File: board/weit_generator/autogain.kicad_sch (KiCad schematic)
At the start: 11 parts, among them U3 TL431DBZ

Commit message: .
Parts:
- removed U3: TL431DBZ, Package_TO_SOT_SMD:SOT-23, symbol Reference_Voltage:TL431DBZ
- removed U? (x2): MCP6004, Package_SO:SOIC-14_3.9x8.7mm_P1.27mm, symbol Amplifier_Operational:MCP6004
- added U1: MCP6004, Package_DIP:DIP-14_W7.62mm_Socket_LongPads, symbol Amplifier_Operational:MCP6004
- added U3: LM4041LP-ADJ, Package_TO_SOT_THT:TO-92_Inline, symbol Reference_Voltage:LM4041LP-ADJ
- C12: footprint (none) -> Capacitor_SMD:C_0805_2012Metric_Pad1.18x1.45mm_HandSolder
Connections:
- net GND: now also U3.3 (A)
- net IN: now also U1.12 (+)
- net at C?.2, D2.1 (K), R?.2: now also U1.13 (-), U1.3 (+)
- net at D2.2 (A): now also U1.14
- net at C12.1, R25.1: now also U1.1
- net at C12.2, C?.1, RV?.2: now also U1.2 (-)
- net at R?.2, RV?.3: now also U3.2 (K)
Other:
- note added: "Low leakage PP capacitor + 1M resistor for stable decay time"
- note removed: "Low leakage PP capacitor + 1M resistor create predictable decay time"

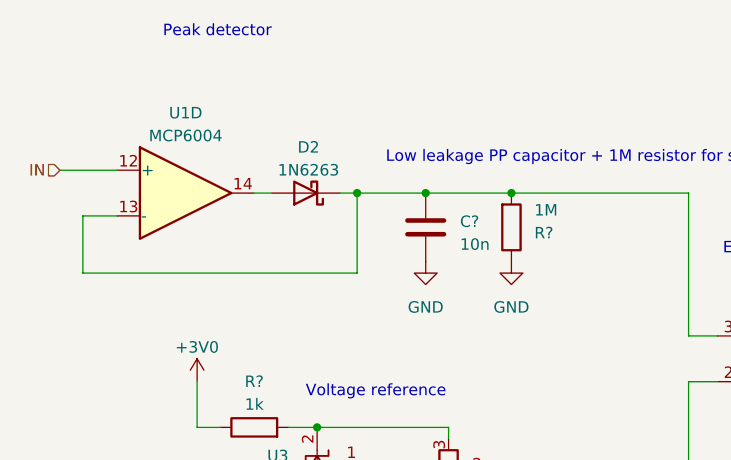
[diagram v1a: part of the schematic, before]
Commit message: added filtering
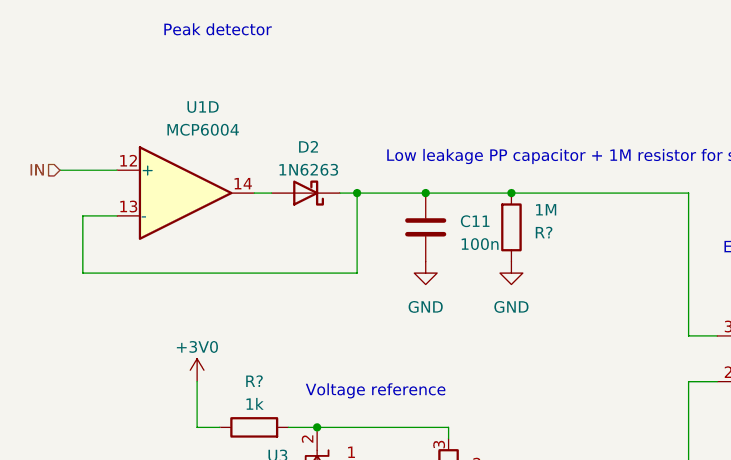
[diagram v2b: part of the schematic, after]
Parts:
- removed C?: 10n, Capacitor_THT:C_Rect_L9.0mm_W4.0mm_P7.50mm_MKT, symbol Device:C
- added C11: 100n, Capacitor_THT:C_Rect_L13.0mm_W6.0mm_P10.00mm_FKS3_FKP3_MKS4, symbol Device:C
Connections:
- net GND: now also C11.1
- net at D2.1 (K), R?.2, U1.13 (-)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: now also C11.2
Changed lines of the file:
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@@
   (junction (at 118.11 77.47) (diameter 0) (color 0 0 0 0)
   )
+  (junction (at 125.73 77.47) (diameter 0) (color 0 0 0 0)
+  )
   (junction (at 154.94 108.585) (diameter 0) (color 0 0 0 0)
   )
-  (junction (at 125.73 77.47) (diameter 0) (color 0 0 0 0)
-  )
   (junction (at 134.62 108.585) (diameter 0) (color 0 0 0 0)
   )
@@
     (stroke (width 0) (type default))
   )
+  (wire (pts (xy 118.11 77.47) (xy 125.73 77.47))
+    (stroke (width 0) (type default))
+  )
+  (wire (pts (xy 134.62 108.585) (xy 154.94 108.585))
+    (stroke (width 0) (type default))
+  )
+  (wire (pts (xy 87.63 86.36) (xy 87.63 80.01))
+    (stroke (width 0) (type default))
+  )
+  (wire (pts (xy 154.94 98.425) (xy 158.115 98.425))
+    (stroke (width 0) (type default))
+  )
+  (wire (pts (xy 169.545 108.585) (xy 175.26 108.585))
+    (stroke (width 0) (type default))
+  )
+  (wire (pts (xy 100.33 103.505) (xy 102.87 103.505))
+    (stroke (width 0) (type default))
+  )
+  (wire (pts (xy 118.11 86.36) (xy 87.63 86.36))
+    (stroke (width 0) (type default))
+  )
+  (wire (pts (xy 87.63 80.01) (xy 91.44 80.01))
+    (stroke (width 0) (type default))
+  )
   (wire (pts (xy 125.73 77.47) (xy 135.255 77.47))
     (stroke (width 0) (type default))
   )
-  (wire (pts (xy 134.62 108.585) (xy 154.94 108.585))
-    (stroke (width 0) (type default))
-  )
-  (wire (pts (xy 87.63 86.36) (xy 87.63 80.01))
-    (stroke (width 0) (type default))
-  )
-  (wire (pts (xy 154.94 98.425) (xy 158.115 98.425))
-    (stroke (width 0) (type default))
-  )
-  (wire (pts (xy 169.545 108.585) (xy 175.26 108.585))
-    (stroke (width 0) (type default))
-  )
-  (wire (pts (xy 100.33 103.505) (xy 102.87 103.505))
-    (stroke (width 0) (type default))
-  )
-  (wire (pts (xy 118.11 86.36) (xy 87.63 86.36))
-    (stroke (width 0) (type default))
-  )
-  (wire (pts (xy 87.63 80.01) (xy 91.44 80.01))
-    (stroke (width 0) (type default))
-  )
   (wire (pts (xy 173.355 95.885) (xy 175.26 95.885))
     (stroke (width 0) (type default))
@@
   )
   (wire (pts (xy 110.49 103.505) (xy 113.665 103.505))
-    (stroke (width 0) (type default))
-  )
-  (wire (pts (xy 118.11 77.47) (xy 125.73 77.47))
     (stroke (width 0) (type default))
   )
@@
   (hierarchical_label "IN" (shape input) (at 85.09 74.93 180) (fields_autoplaced)
     (effects (font (size 1.27 1.27)) (justify right))
+  )
+  (symbol (lib_id "Device:C") (at 125.73 81.28 180) (unit 1)
+    (in_bom yes) (on_board yes) (dnp no) (fields_autoplaced)
+    (property "Reference" "C11" (at 129.54 80.645 0)
+      (effects (font (size 1.27 1.27)) (justify right))
+    )
+    (property "Value" "100n" (at 129.54 83.185 0)
+      (effects (font (size 1.27 1.27)) (justify right))
+    )
+    (property "Footprint" "Capacitor_THT:C_Rect_L13.0mm_W6.0mm_P10.00mm_FKS3_FKP3_MKS4" (at 124.7648 77.47 0)
+      (effects (font (size 1.27 1.27)) hide)
+    )
+    (property "Datasheet" "~" (at 125.73 81.28 0)
+      (effects (font (size 1.27 1.27)) hide)
+    )
+    (pin "1")
+    (pin "2")
+    (instances
+      (project "weit_generator"
+        (path "/b85c55a9-e1f6-4dbf-a795-73634abf8d52"
+          (reference "C11") (unit 1)
+        )
+        (path "/b85c55a9-e1f6-4dbf-a795-73634abf8d52/97b440c2-49e0-43c1-8dbd-070a3fa32fe0"
+          (reference "C6") (unit 1)
+        )
+      )
+    )
   )
   (symbol (lib_id "Diode:1N6263") (at 112.395 77.47 180) (unit 1)
@@
   )
   (symbol (lib_id "Amplifier_Operational:MCP6004") (at 99.06 77.47 0) (unit 4)
-    (in_bom yes) (on_board yes) (dnp no) (fields_autoplaced)
-    (property "Reference" "U1" (at 99.06 68.58 0)
-      (effects (font (size 1.27 1.27)))
-    )
-    (property "Value" "MCP6004" (at 99.06 71.12 0)
+    (in_bom yes) (on_board yes) (dnp no)
+    (property "Reference" "U1" (at 100.965 67.945 0)
+      (effects (font (size 1.27 1.27)))
+    )
+    (property "Value" "MCP6004" (at 100.965 70.485 0)
       (effects (font (size 1.27 1.27)))
     )
@@
         )
       )
-    )
-  )
-  (symbol (lib_id "Device:C") (at 125.73 81.28 180) (unit 1)
-    (in_bom yes) (on_board yes) (dnp no)
-    (property "Reference" "C?" (at 129.54 80.645 0)
-      (effects (font (size 1.27 1.27)) (justify right))
-    )
-    (property "Value" "10n" (at 129.54 83.185 0)
-      (effects (font (size 1.27 1.27)) (justify right))
-    )
-    (property "Footprint" "Capacitor_THT:C_Rect_L9.0mm_W4.0mm_P7.50mm_MKT" (at 124.7648 77.47 0)
-      (effects (font (size 1.27 1.27)) hide)
-    )
-    (property "Datasheet" "~" (at 125.73 81.28 0)
-      (effects (font (size 1.27 1.27)) hide)
-    )
-    (pin "1")
-    (pin "2")
-    (instances
-      (project "weit_generator"
-        (path "/b85c55a9-e1f6-4dbf-a795-73634abf8d52"
-          (reference "C?") (unit 1)
-        )
-        (path "/b85c55a9-e1f6-4dbf-a795-73634abf8d52/97b440c2-49e0-43c1-8dbd-070a3fa32fe0"
-          (reference "C9") (unit 1)
-        )
-      )

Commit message: hopefully repaired instability
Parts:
- removed C12: 1n, Capacitor_SMD:C_0805_2012Metric_Pad1.18x1.45mm_HandSolder, symbol Device:C
- removed C?: 100n, Capacitor_SMD:C_0805_2012Metric_Pad1.18x1.45mm_HandSolder, symbol Device:C
- removed R?: 1k, Resistor_SMD:R_0805_2012Metric_Pad1.20x1.40mm_HandSolder, symbol Device:R
- removed RV?: 10k, Potentiometer_THT:Potentiometer_Bourns_3266Y_Vertical, symbol Device:R_Potentiometer
- removed U3: LM4041LP-ADJ, Package_TO_SOT_THT:TO-92_Inline, symbol Reference_Voltage:LM4041LP-ADJ
- added C7: 100u, symbol Device:C_Polarized
- added C?: 10n, Capacitor_THT:C_Rect_L9.0mm_W4.0mm_P7.50mm_MKT, symbol Device:C
- added Q1: BC547, Package_TO_SOT_THT:TO-92_Inline, symbol Transistor_BJT:BC547
- added R21: 100k, Resistor_THT:R_Axial_DIN0207_L6.3mm_D2.5mm_P2.54mm_Vertical, symbol Device:R
- added R?: 1M, Resistor_THT:R_Axial_DIN0207_L6.3mm_D2.5mm_P2.54mm_Vertical, symbol Device:R
- added R? (x2): 100k, Resistor_SMD:R_0805_2012Metric_Pad1.20x1.40mm_HandSolder, symbol Device:R
- added RV?: 10k, Potentiometer_THT:Potentiometer_Bourns_3266Y_Vertical, symbol Device:R_Potentiometer
- C11: value 100n -> 10n
- R25: value 1k -> 100
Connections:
- net GND: now also C7.2, Q1.3 (E), R?.1, R?.1
- net IN: now also C?.2; no longer U1.12 (+)
- net OUT: now also R25.1; no longer R25.2
- net at U1.1: now also RV?.2; no longer R25.1
- net Vref: now reaches U1.2 (-)
- new net: C7.1, R21.1, R?.2, RV?.3
- new net: C?.1, R?.2, R?.2, U1.12 (+)
- new net: Q1.1 (C), R25.2
- new net: Q1.2 (B), R21.2
- new net +1V2: R?.1
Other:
- note removed: "Voltage reference"
- moved on the sheet: R25, R?

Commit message: New layout
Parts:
- removed C?: 10n, Capacitor_THT:C_Rect_L9.0mm_W4.0mm_P7.50mm_MKT, symbol Device:C
- removed R? (x2): 100k, Resistor_SMD:R_0805_2012Metric_Pad1.20x1.40mm_HandSolder, symbol Device:R
- removed U1: MCP6004, Package_DIP:DIP-14_W7.62mm_Socket_LongPads, symbol Amplifier_Operational:MCP6004
- added C11: 1u, Capacitor_THT:C_Rect_L7.2mm_W4.5mm_P5.00mm_FKS2_FKP2_MKS2_MKP2, symbol Device:C
- added C12: 22u, Capacitor_THT:CP_Radial_D6.3mm_P2.50mm, symbol Device:C_Polarized
- added R24: 100, Resistor_THT:R_Axial_DIN0207_L6.3mm_D2.5mm_P2.54mm_Vertical, symbol Device:R
- added R26: 10k, Resistor_THT:R_Axial_DIN0207_L6.3mm_D2.5mm_P2.54mm_Vertical, symbol Device:R
- added R?: 1M, Resistor_THT:R_Axial_DIN0207_L6.3mm_D2.5mm_P2.54mm_Vertical, symbol Device:R
- added RV1: 10k, Potentiometer_THT:Potentiometer_Bourns_3266Y_Vertical, symbol Device:R_Potentiometer
- added TP1 (x2): TestPoint, TestPoint:TestPoint_Pad_D3.0mm, symbol Connector:TestPoint
- added U? (x2): MCP6004, Package_DIP:DIP-14_W7.62mm_Socket, symbol Amplifier_Operational:MCP6004
- C13: renamed from C7; footprint (none) -> Capacitor_THT:CP_Radial_D6.3mm_P2.50mm
- C?: renamed from C11; footprint Capacitor_THT:C_Rect_L13.0mm_W6.0mm_P10.00mm_FKS3_FKP3_MKS4 -> Capacitor_THT:C_Rect_L13.0mm_W4.0mm_P10.00mm_FKS3_FKP3_MKS4; Dielectric (none) -> Polistyrene
- R28: renamed from R21; value 100k -> 100
- renumbered R25 to R29
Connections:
- net +1V2: now also RV1.3
- net GND: now also RV1.1
- net IN: now also R?.2
- net at C?.2, R?.2: now also R24.2, TP1.1, U?.10 (+); no longer D2.1 (K)
- net at C13.1, R28.1, R?.2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: now also TP1.1
- net at D2.2 (A): now also U?.14
- net at RV?.2: now also C11.2, C12.1, U?.8
- new net: D2.1 (K), R24.1, U?.13 (-)
- new net: C12.2, R26.1
- new net: C11.1, R26.2, RV1.2, U?.9 (-)
- new net: R?.1, U?.12 (+)
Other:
- note added: "Compensation Network"
- note added: "RV2 sets coupling strength"
- note removed: "Low leakage PP capacitor + 1M resistor for stable decay time"
- moved on the sheet: C13, C?, D2, Q1, R28, R29, R?, RV?

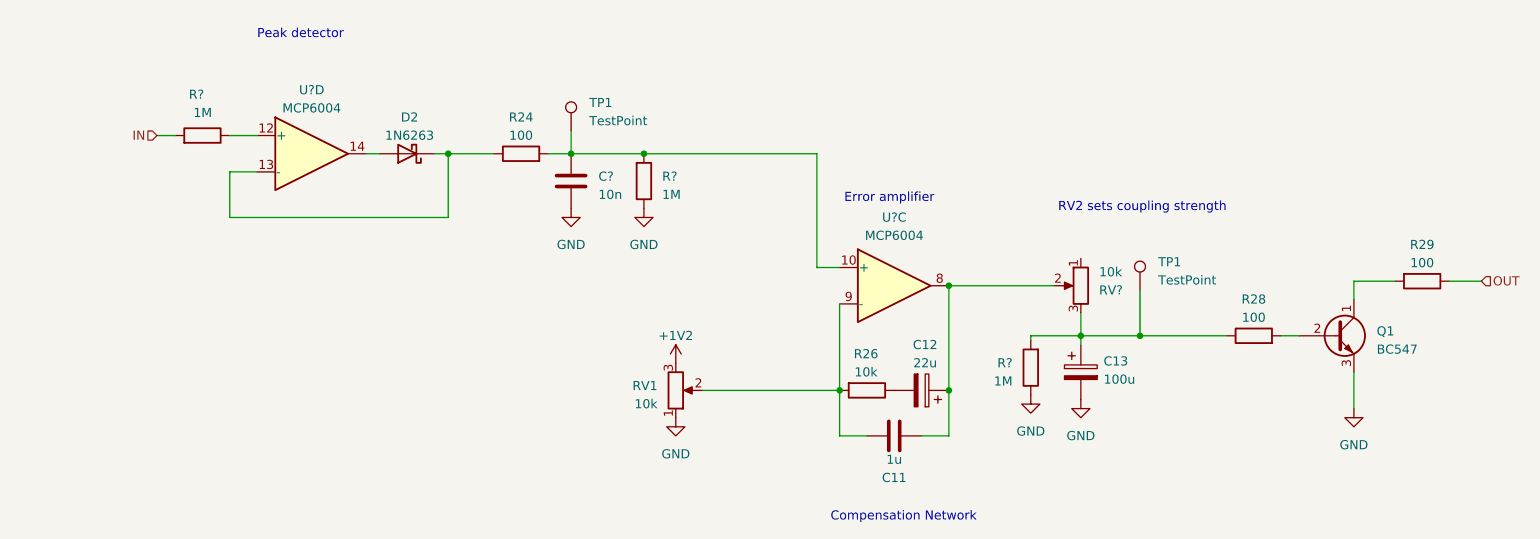
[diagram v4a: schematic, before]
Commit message: finished board, added test desription and tuning to docs
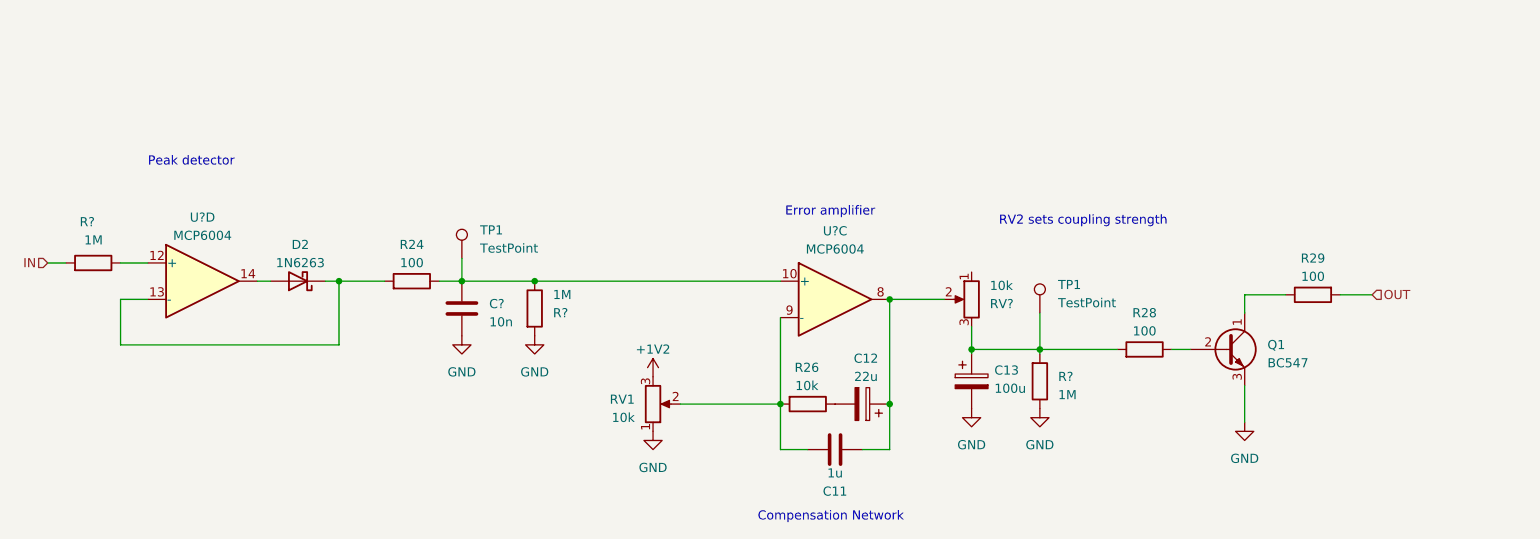
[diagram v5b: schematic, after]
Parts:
- TP1: footprint TestPoint:TestPoint_Pad_D3.0mm -> TestPoint:TestPoint_Pad_D2.0mm
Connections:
- net GND: now also R?.2; no longer R?.1
- net OUT: now also R29.2; no longer R29.1
- net at C?.2, TP1.1, U?.10 (+): now also R24.1, R?.1; no longer R24.2, R?.2
- net at C13.1, R?.2, RV?.3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: now also R28.2; no longer R28.1
- net at D2.1 (K), U?.13 (-): now also R24.2; no longer R24.1
- net at Q1.1 (C): now also R29.1; no longer R29.2
- net at Q1.2 (B): now also R28.1; no longer R28.2
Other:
- moved on the sheet: C11, C12, C13, C?, D2, Q1, R24, R26, R28, R29, R?, RV1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

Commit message: .
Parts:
- renumbered C13 to C11, C11 to C9, R29 to R24, R26 to R25, R28 to R26, R24 to R28
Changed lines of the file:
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@@
         )
         (path "/b85c55a9-e1f6-4dbf-a795-73634abf8d52/97b440c2-49e0-43c1-8dbd-070a3fa32fe0"
-          (reference "C10") (unit 1)
+          (reference "C13") (unit 1)
         )
       )
@@
   (symbol (lib_id "Device:R") (at 153.67 112.395 270) (unit 1)
     (in_bom yes) (on_board yes) (dnp no)
-    (property "Reference" "R26" (at 153.543 107.315 90)
+    (property "Reference" "R25" (at 153.543 107.315 90)
       (effects (font (size 1.27 1.27)))
     )
@@
       (project "weit_generator"
         (path "/b85c55a9-e1f6-4dbf-a795-73634abf8d52/97b440c2-49e0-43c1-8dbd-070a3fa32fe0"
-          (reference "R26") (unit 1)
+          (reference "R25") (unit 1)
         )
       )
@@
         )
         (path "/b85c55a9-e1f6-4dbf-a795-73634abf8d52/97b440c2-49e0-43c1-8dbd-070a3fa32fe0"
-          (reference "U1") (unit 3)
+          (reference "U2") (unit 3)
         )
       )
@@
         )
         (path "/b85c55a9-e1f6-4dbf-a795-73634abf8d52/97b440c2-49e0-43c1-8dbd-070a3fa32fe0"
-          (reference "R25") (unit 1)
+          (reference "R29") (unit 1)
         )
       )
@@
         )
         (path "/b85c55a9-e1f6-4dbf-a795-73634abf8d52/97b440c2-49e0-43c1-8dbd-070a3fa32fe0"
-          (reference "R23") (unit 1)
+          (reference "R22") (unit 1)
         )
       )
@@
   (symbol (lib_id "Device:C") (at 157.48 118.745 90) (mirror x) (unit 1)
     (in_bom yes) (on_board yes) (dnp no)
-    (property "Reference" "C11" (at 157.48 124.587 90)
+    (property "Reference" "C9" (at 157.48 124.587 90)
       (effects (font (size 1.27 1.27)))
     )
@@
       (project "weit_generator"
         (path "/b85c55a9-e1f6-4dbf-a795-73634abf8d52/97b440c2-49e0-43c1-8dbd-070a3fa32fe0"
-          (reference "C11") (unit 1)
+          (reference "C9") (unit 1)
         )
       )
@@
   (symbol (lib_id "Device:C_Polarized") (at 176.53 109.22 0) (unit 1)
     (in_bom yes) (on_board yes) (dnp no) (fields_autoplaced)
-    (property "Reference" "C13" (at 179.705 107.696 0)
+    (property "Reference" "C11" (at 179.705 107.696 0)
       (effects (font (size 1.27 1.27)) (justify left))
     )
@@
       (project "weit_generator"
         (path "/b85c55a9-e1f6-4dbf-a795-73634abf8d52/97b440c2-49e0-43c1-8dbd-070a3fa32fe0"
-          (reference "C13") (unit 1)
+          (reference "C11") (unit 1)
         )
       )
@@
   (symbol (lib_id "Device:R") (at 98.425 95.25 270) (mirror x) (unit 1)
     (in_bom yes) (on_board yes) (dnp no)
-    (property "Reference" "R24" (at 98.425 90.17 90)
+    (property "Reference" "R28" (at 98.425 90.17 90)
       (effects (font (size 1.27 1.27)))
     )
@@
       (project "weit_generator"
         (path "/b85c55a9-e1f6-4dbf-a795-73634abf8d52/97b440c2-49e0-43c1-8dbd-070a3fa32fe0"
+          (reference "R28") (unit 1)
+        )
+      )
+    )
+  )
+  (symbol (lib_id "Device:R") (at 224.155 97.155 90) (mirror x) (unit 1)
+    (in_bom yes) (on_board yes) (dnp no)
+    (property "Reference" "R24" (at 224.155 92.075 90)
+      (effects (font (size 1.27 1.27)))
+    )
+    (property "Value" "100" (at 224.155 94.615 90)
+      (effects (font (size 1.27 1.27)))
+    )
+    (property "Footprint" "Resistor_THT:R_Axial_DIN0207_L6.3mm_D2.5mm_P2.54mm_Vertical" (at 224.155 95.377 90)
+      (effects (font (size 1.27 1.27)) hide)
+    )
+    (property "Datasheet" "~" (at 224.155 97.155 0)
+      (effects (font (size 1.27 1.27)) hide)
+    )
+    (pin "1")
+    (pin "2")
+    (instances
+      (project "weit_generator"
+        (path "/b85c55a9-e1f6-4dbf-a795-73634abf8d52/97b440c2-49e0-43c1-8dbd-070a3fa32fe0"
           (reference "R24") (unit 1)
-        )
-      )
-    )
-  )
-  (symbol (lib_id "Device:R") (at 224.155 97.155 90) (mirror x) (unit 1)
-    (in_bom yes) (on_board yes) (dnp no)
-    (property "Reference" "R29" (at 224.155 92.075 90)
-      (effects (font (size 1.27 1.27)))
-    )
-    (property "Value" "100" (at 224.155 94.615 90)
-      (effects (font (size 1.27 1.27)))
-    )
-    (property "Footprint" "Resistor_THT:R_Axial_DIN0207_L6.3mm_D2.5mm_P2.54mm_Vertical" (at 224.155 95.377 90)
-      (effects (font (size 1.27 1.27)) hide)
-    )
-    (property "Datasheet" "~" (at 224.155 97.155 0)
-      (effects (font (size 1.27 1.27)) hide)
-    )
-    (pin "1")
-    (pin "2")
-    (instances
-      (project "weit_generator"
-        (path "/b85c55a9-e1f6-4dbf-a795-73634abf8d52/97b440c2-49e0-43c1-8dbd-070a3fa32fe0"
-          (reference "R29") (unit 1)
         )
       )
@@
   (symbol (lib_id "Device:R") (at 200.66 104.775 270) (mirror x) (unit 1)
     (in_bom yes) (on_board yes) (dnp no)
-    (property "Reference" "R28" (at 200.66 99.695 90)
+    (property "Reference" "R26" (at 200.66 99.695 90)
       (effects (font (size 1.27 1.27)))
     )
@@
       (project "weit_generator"
         (path "/b85c55a9-e1f6-4dbf-a795-73634abf8d52/97b440c2-49e0-43c1-8dbd-070a3fa32fe0"
-          (reference "R28") (unit 1)
+          (reference "R26") (unit 1)
         )
       )
@@
         )
         (path "/b85c55a9-e1f6-4dbf-a795-73634abf8d52/97b440c2-49e0-43c1-8dbd-070a3fa32fe0"
-          (reference "U1") (unit 4)
-        )
-      )
+          (reference "U2") (unit 4)
+        )
+      )

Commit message: .
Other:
- moved on the sheet: C11, C12, C9, C?, D2, Q1, R24, R25, R26, R28, R?, RV1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

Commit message: WIELKA POLONIAAAAA
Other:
- note added: "Detektro szczytowy"
- note added: "RV2 dostraja siłę sprzężenia"
- note added: "Sieć kompensacyjna"
- note added: "Wzmacniacz błędu"
- note removed: "Compensation Network"
- note removed: "Error amplifier"
- note removed: "Peak detector"
- note removed: "RV2 sets coupling strength"
- title: (none) -> Automatyczna kontrola amplitudy
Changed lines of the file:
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@@
 (kicad_sch (version 20230121) (generator eeschema)
   (paper "A4")
+  (title_block
+    (title "Automatyczna kontrola amplitudy")
+    (date "2023-04-15")
+    (rev "1.0")
+    (comment 1 "Kondensatory polipropylenowe/polisertynowe")
+  )
   (junction (at 171.45 112.395) (diameter 0) (color 0 0 0 0)
   )
@@
     (stroke (width 0) (type default))
   )
-  (text "Error amplifier" (at 156.845 86.36 0)
+  (text "Wzmacniacz błędu" (at 156.845 86.36 0)
     (effects (font (size 1.27 1.27)) (justify left bottom))
   )
-  (text "RV2 sets coupling strength" (at 186.69 87.63 0)
+  (text "RV2 dostraja siłę sprzężenia" (at 186.69 87.63 0)
     (effects (font (size 1.27 1.27)) (justify left bottom))
   )
-  (text "Compensation Network" (at 153.035 128.905 0)
+  (text "Sieć kompensacyjna\n" (at 153.035 128.905 0)
     (effects (font (size 1.27 1.27)) (justify left bottom))
   )
-  (text "Peak detector\n" (at 73.66 79.375 0)
+  (text "Detektro szczytowy\n" (at 74.295 81.915 0)
     (effects (font (size 1.27 1.27)) (justify left bottom))
   )
